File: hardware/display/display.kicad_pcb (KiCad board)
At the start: 4 copper layers, 98 x 67 mm, 420 parts, among them J1 Power Connector, J2 Data Connector

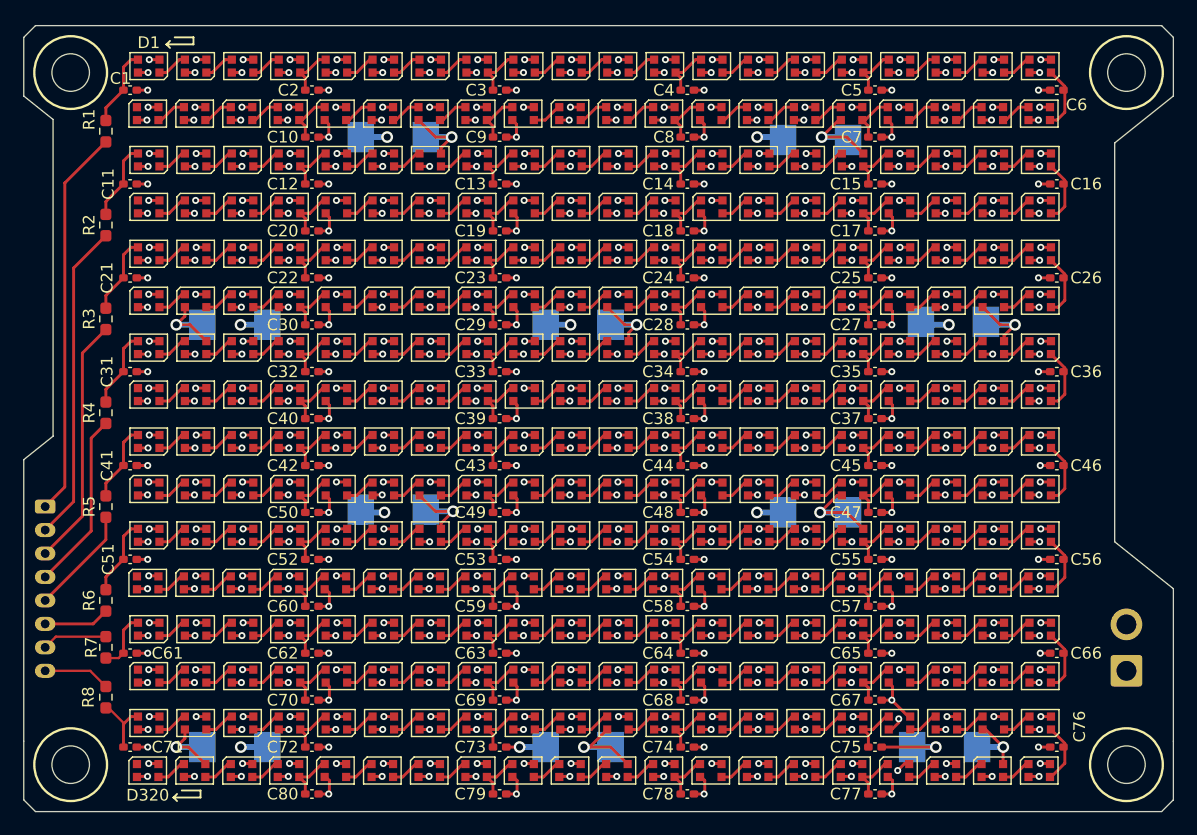
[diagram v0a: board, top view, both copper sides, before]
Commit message: Added Real Mounting Holes and Fiducial
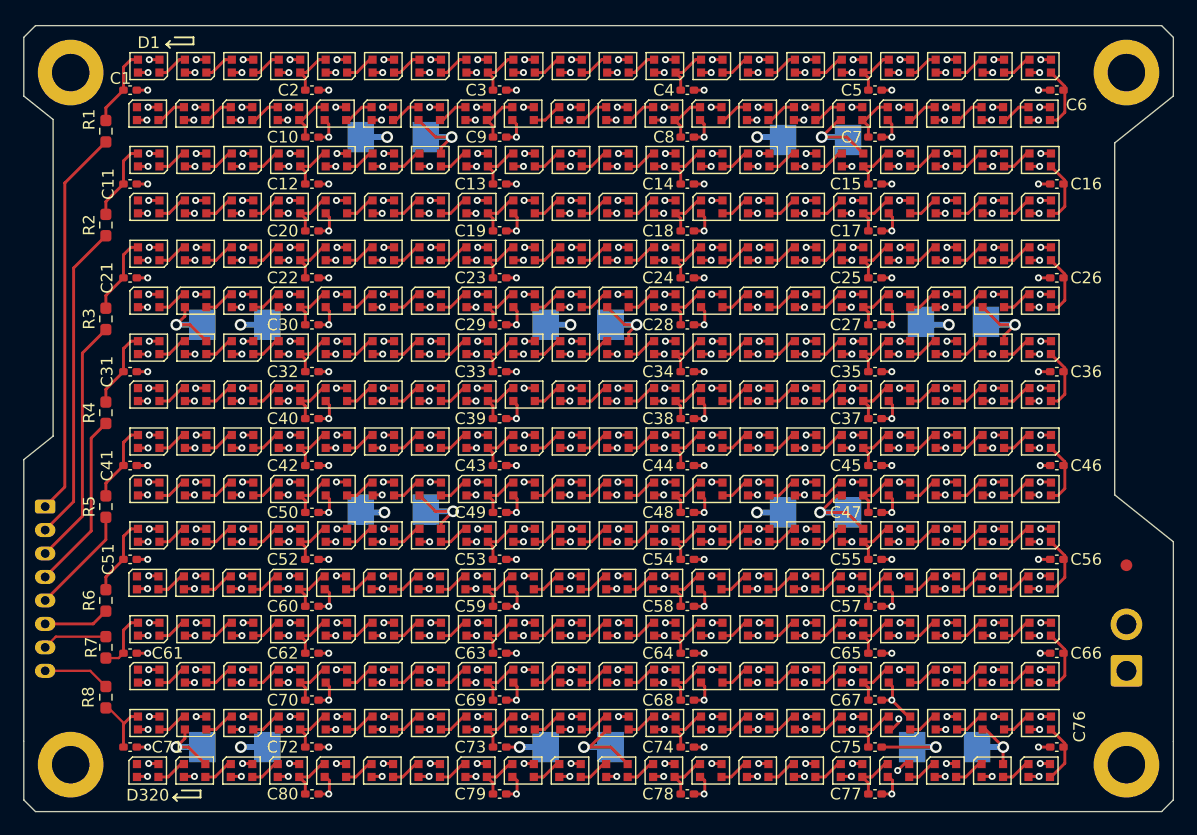
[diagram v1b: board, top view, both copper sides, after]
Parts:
- added FID2: Fiducial, Fiducial:Fiducial_1mm_Mask2mm, F.Cu at (101.0, 58.0)
- added H1: MountingHole, MountingHole:MountingHole_3.2mm_M3_DIN965_Pad, F.Cu at (11.0, 16.0)
- added H2: MountingHole, MountingHole:MountingHole_3.2mm_M3_DIN965_Pad, F.Cu at (101.0, 16.0)
- added H3: MountingHole, MountingHole:MountingHole_3.2mm_M3_DIN965_Pad, F.Cu at (11.0, 75.0)
- added H4: MountingHole, MountingHole:MountingHole_3.2mm_M3_DIN965_Pad, F.Cu at (101.0, 75.0)
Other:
- outline, holes or cut-outs redrawn

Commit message: Updated Mounting Holes
M2 screw holes for M2x4mm screws into top of case.
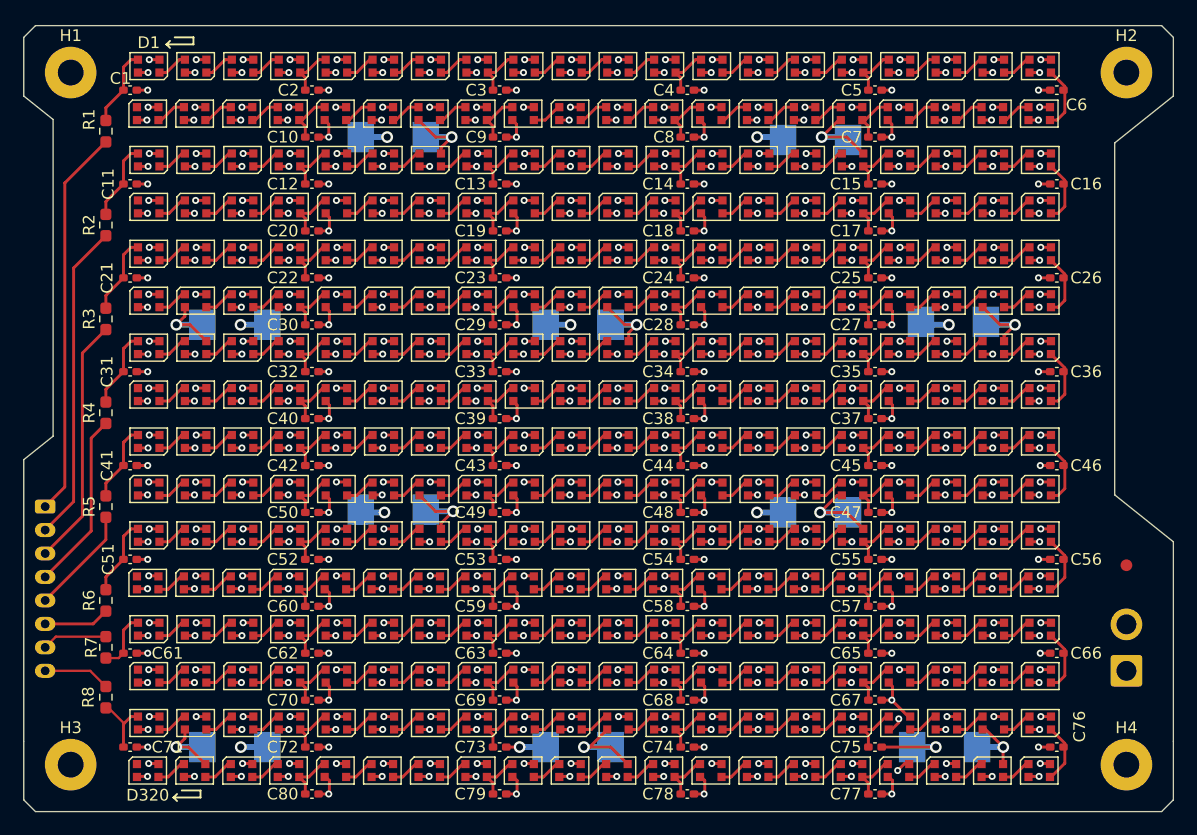
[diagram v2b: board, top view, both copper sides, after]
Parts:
- removed FID2: Fiducial, Fiducial:Fiducial_1mm_Mask2mm
- added FID1: Fiducial, Fiducial:Fiducial_1mm_Mask2mm, F.Cu at (101.0, 58.0)
- H1, H2, H3, H4: footprint MountingHole:MountingHole_3.2mm_M3_DIN965_Pad -> MountingHole:MountingHole_2.2mm_M2_Pad
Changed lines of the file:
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@@
 		)
 	)
-	(footprint "MountingHole:MountingHole_3.2mm_M3_DIN965_Pad"
+	(footprint "MountingHole:MountingHole_2.2mm_M2_Pad"
 		(layer "F.Cu")
 		(at 101 75)
-		(descr "Mounting Hole 3.2mm, M3, generated by kicad-footprint-generator mountinghole.py")
-		(tags "mountinghole M3 DIN965")
+		(descr "Mounting Hole 2.2mm, M2, generated by kicad-footprint-generator mountinghole.py")
+		(tags "mountinghole M2")
 		(property "Reference" "H4"
-			(at 0 -3.75 0)
+			(at 0 -3.15 0)
 			(layer "F.SilkS")
-			(hide yes)
 			(effects
 				(font
@@
 		)
 		(property "Value" "MountingHole"
-			(at 0 3.75 0)
+			(at 0 3.15 0)
 			(layer "F.Fab")
 			(effects
@@
 		(fp_circle
 			(center 0 0)
-			(end 2.8 0)
+			(end 2.2 0)
 			(stroke
 				(width 0.15)
@@
 		(fp_circle
 			(center 0 0)
-			(end 3.05 0)
+			(end 2.45 0)
 			(stroke
 				(width 0.05)
@@
 		(pad "1" thru_hole circle
 			(at 0 0)
-			(size 5.6 5.6)
-			(drill 3.2)
+			(size 4.4 4.4)
+			(drill 2.2)
 			(layers "*.Cu" "*.Mask")
 			(remove_unused_layers no)
@@
 		)
 	)
-	(footprint "MountingHole:MountingHole_3.2mm_M3_DIN965_Pad"
+	(footprint "MountingHole:MountingHole_2.2mm_M2_Pad"
 		(layer "F.Cu")
 		(at 11 75)
-		(descr "Mounting Hole 3.2mm, M3, generated by kicad-footprint-generator mountinghole.py")
-		(tags "mountinghole M3 DIN965")
+		(descr "Mounting Hole 2.2mm, M2, generated by kicad-footprint-generator mountinghole.py")
+		(tags "mountinghole M2")
 		(property "Reference" "H3"
-			(at 0 -3.75 0)
+			(at 0 -3.15 0)
 			(layer "F.SilkS")
-			(hide yes)
 			(effects
 				(font
@@
 		)
 		(property "Value" "MountingHole"
-			(at 0 3.75 0)
+			(at 0 3.15 0)
 			(layer "F.Fab")
 			(effects
@@
 		(fp_circle
 			(center 0 0)
-			(end 2.8 0)
+			(end 2.2 0)
 			(stroke
 				(width 0.15)
@@
 		(fp_circle
 			(center 0 0)
-			(end 3.05 0)
+			(end 2.45 0)
 			(stroke
 				(width 0.05)
@@
 		(pad "1" thru_hole circle
 			(at 0 0)
-			(size 5.6 5.6)
-			(drill 3.2)
+			(size 4.4 4.4)
+			(drill 2.2)
 			(layers "*.Cu" "*.Mask")
 			(remove_unused_layers no)
@@
 		)
 	)
-	(footprint "Fiducial:Fiducial_1mm_Mask2mm"
-		(layer "F.Cu")
-		(at 101 58)
-		(descr "Fiducial, circular marking, 1mm bare copper, 2mm soldermask opening (Level A)")
-		(tags "fiducial")
-		(property "Reference" "FID2"
-			(at 0 -1.95 0)
-			(layer "F.SilkS")
-			(hide yes)
-			(effects
-				(font
-					(size 1 1)
-					(thickness 0.15)
-				)
-			)
-		)
-		(property "Value" "Fiducial"
-			(at 0 1.95 0)
-			(layer "F.Fab")
-			(effects
-				(font
-					(size 1 1)
-					(thickness 0.15)
-				)
-			)
-		)
-		(property "Datasheet" "~"
-			(at 0 0 0)
-			(layer "F.Fab")
-			(hide yes)
-			(effects
-				(font
-					(size 1.27 1.27)
-					(thickness 0.15)
-				)
-			)
-		)
-		(property "Description" "Fiducial Marker"
-			(at 0 0 0)
-			(layer "F.Fab")
-			(hide yes)
-			(effects
-				(font
-					(size 1.27 1.27)
-					(thickness 0.15)
-				)
-			)
-		)
-		(property ki_fp_filters "Fiducial*")
-		(sheetname "/")
-		(sheetfile "display.kicad_sch")
-		(attr smd exclude_from_bom)
-		(fp_circle
-			(center 0 0)
-			(end 1.25 0)
-			(stroke
-				(width 0.05)
-				(type solid)
-			)
-			(fill no)
-			(layer "F.CrtYd")
-		)
-		(fp_circle
-			(center 0 0)
-			(end 1 0)
-			(stroke
-				(width 0.1)
-				(type solid)
-			)
-			(fill no)
-			(layer "F.Fab")
-		)
-		(fp_text user "${REFERENCE}"
-			(at 0 0 0)
-			(layer "F.Fab")
-			(effects
-				(font
-					(size 0.5 0.5)
-					(thickness 0.08)
-				)
-			)
-		)
-		(pad "" smd circle
-			(at 0 0)
-			(size 1 1)
-			(layers "F.Cu" "F.Mask")
-			(solder_mask_margin 0.5)
-			(clearance 0.6)
-		)
-		(embedded_fonts no)
-	)
 	(footprint "Capacitor_SMD:C_0402_1005Metric_Pad0.74x0.62mm_HandSolder"
 		(layer "F.Cu")
@@
 		)
 	)
-	(footprint "MountingHole:MountingHole_3.2mm_M3_DIN965_Pad"
+	(footprint "MountingHole:MountingHole_2.2mm_M2_Pad"
 		(layer "F.Cu")
 		(at 11 16)
-		(descr "Mounting Hole 3.2mm, M3, generated by kicad-footprint-generator mountinghole.py")
-		(tags "mountinghole M3 DIN965")
+		(descr "Mounting Hole 2.2mm, M2, generated by kicad-footprint-generator mountinghole.py")
+		(tags "mountinghole M2")
 		(property "Reference" "H1"
-			(at 0 -3.75 0)
+			(at 0 -3.15 0)
 			(layer "F.SilkS")
-			(hide yes)
 			(effects
 				(font
@@
 		)
 		(property "Value" "MountingHole"
-			(at 0 3.75 0)
+			(at 0 3.15 0)
 			(layer "F.Fab")
 			(effects
@@
 		(fp_circle
 			(center 0 0)
-			(end 2.8 0)
+			(end 2.2 0)
 			(stroke
 				(width 0.15)
@@
 		(fp_circle
 			(center 0 0)
-			(end 3.05 0)
+			(end 2.45 0)
 			(stroke
 				(width 0.05)
@@
 		(pad "1" thru_hole circle
 			(at 0 0)
-			(size 5.6 5.6)
-			(drill 3.2)
+			(size 4.4 4.4)
+			(drill 2.2)
 			(layers "*.Cu" "*.Mask")
 			(remove_unused_layers no)
@@
 		)
 	)
-	(footprint "MountingHole:MountingHole_3.2mm_M3_DIN965_Pad"
+	(footprint "MountingHole:MountingHole_2.2mm_M2_Pad"
 		(layer "F.Cu")
 		(at 101 16)
-		(descr "Mounting Hole 3.2mm, M3, generated by kicad-footprint-generator mountinghole.py")
-		(tags "mountinghole M3 DIN965")
+		(descr "Mounting Hole 2.2mm, M2, generated by kicad-footprint-generator mountinghole.py")
+		(tags "mountinghole M2")
 		(property "Reference" "H2"
-			(at 0 -3.75 0)
+			(at 0 -3.15 0)
 			(layer "F.SilkS")
-			(hide yes)
 			(effects
 				(font
@@
 		)
 		(property "Value" "MountingHole"
-			(at 0 3.75 0)
+			(at 0 3.15 0)
 			(layer "F.Fab")
 			(effects
@@
 		(fp_circle
 			(center 0 0)
-			(end 2.8 0)
+			(end 2.2 0)
 			(stroke
 				(width 0.15)
@@
 		(fp_circle
 			(center 0 0)
-			(end 3.05 0)
+			(end 2.45 0)
 			(stroke
 				(width 0.05)
@@
 		(pad "1" thru_hole circle
 			(at 0 0)
-			(size 5.6 5.6)
-			(drill 3.2)
+			(size 4.4 4.4)
+			(drill 2.2)
 			(layers "*.Cu" "*.Mask")
 			(remove_unused_layers no)
@@
 		)
 	)
+	(footprint "Fiducial:Fiducial_1mm_Mask2mm"
+		(layer "F.Cu")
+		(at 101 58)
+		(descr "Fiducial, circular marking, 1mm bare copper, 2mm soldermask opening (Level A)")
+		(tags "fiducial")
+		(property "Reference" "FID1"
+			(at 0 -1.95 0)
+			(layer "F.SilkS")
+			(hide yes)
+			(effects
+				(font
+					(size 1 1)
+					(thickness 0.15)
+				)
+			)
+		)
+		(property "Value" "Fiducial"
+			(at 0 1.95 0)
+			(layer "F.Fab")
+			(effects
+				(font
+					(size 1 1)
+					(thickness 0.15)
+				)
+			)
+		)
+		(property "Datasheet" "~"
+			(at 0 0 0)
+			(layer "F.Fab")
+			(hide yes)
+			(effects
+				(font
+					(size 1.27 1.27)
+					(thickness 0.15)
+				)
+			)
+		)
+		(property "Description" "Fiducial Marker"
+			(at 0 0 0)
+			(layer "F.Fab")
+			(hide yes)
+			(effects
+				(font
+					(size 1.27 1.27)
+					(thickness 0.15)
+				)
+			)
+		)
+		(property ki_fp_filters "Fiducial*")
+		(sheetname "/")
+		(sheetfile "display.kicad_sch")
+		(attr smd exclude_from_bom)
+		(fp_circle
+			(center 0 0)
+			(end 1.25 0)
+			(stroke
+				(width 0.05)
+				(type solid)
+			)
+			(fill no)
+			(layer "F.CrtYd")
+		)
+		(fp_circle
+			(center 0 0)
+			(end 1 0)
+			(stroke
+				(width 0.1)
+				(type solid)
+			)
+			(fill no)
+			(layer "F.Fab")
+		)
+		(fp_text user "${REFERENCE}"
+			(at 0 0 0)
+			(layer "F.Fab")
+			(effects
+				(font
+					(size 0.5 0.5)
+					(thickness 0.08)
+				)
+			)
+		)
+		(pad "" smd circle
+			(at 0 0)
+			(size 1 1)
+			(layers "F.Cu" "F.Mask")
+			(solder_mask_margin 0.5)
+			(clearance 0.6)
+		)
+		(embedded_fonts no)
+	)
 	(footprint "LED_SMD:LED_WS2812B-2020_PLCC4_2.0x2.0mm"
